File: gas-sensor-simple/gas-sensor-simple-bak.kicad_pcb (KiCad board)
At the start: 2 copper layers, 91.4 x 99.1 mm, 43 parts, among them J1 2x5 pin, J2 2x5 socket, J3 2x5 pin, J4 1x2, J5 1x2, J6 1x2, J7 1x2, U1 MQ-8, U10 RG LED, U12 LM393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

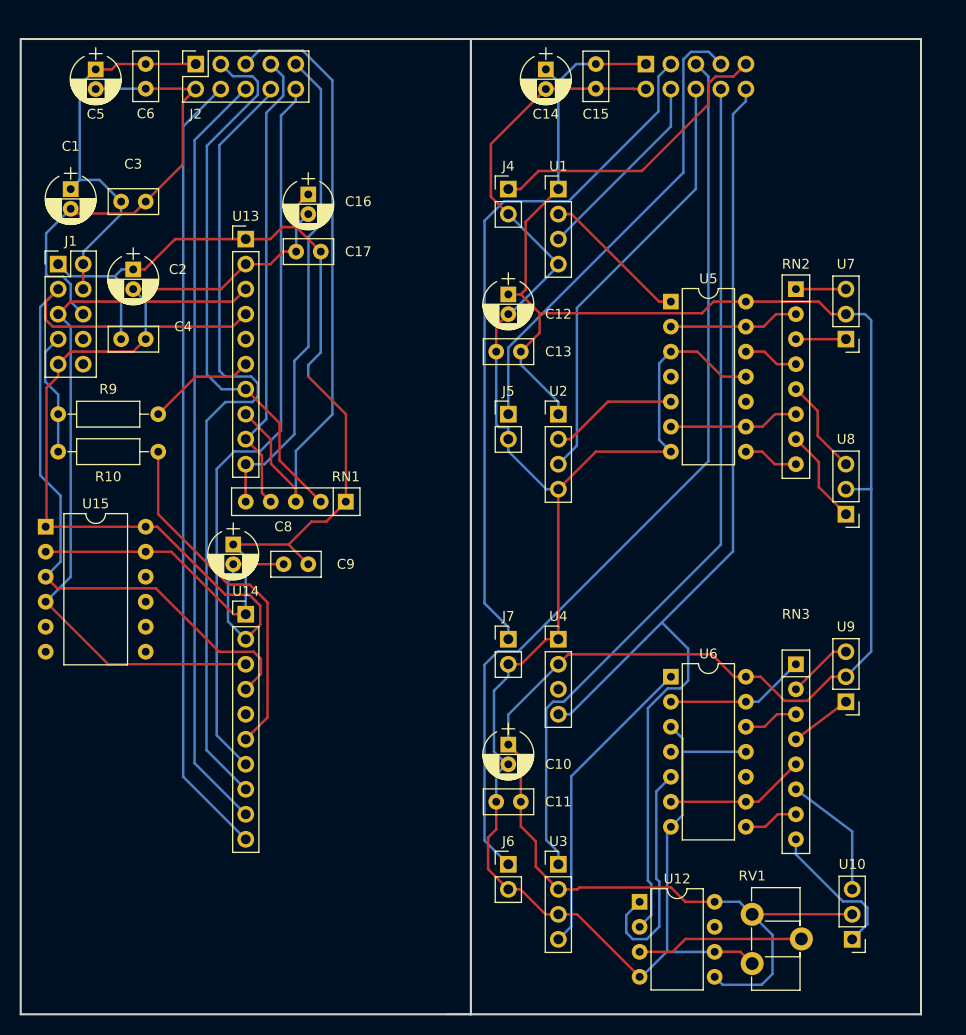
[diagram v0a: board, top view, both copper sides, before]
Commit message: Autorouted version 1 (gas-sensor-simple.kicad_pcb). Start work on version 2 layout (layout.kicad_pcb) moving RPi connector to top of digital board.
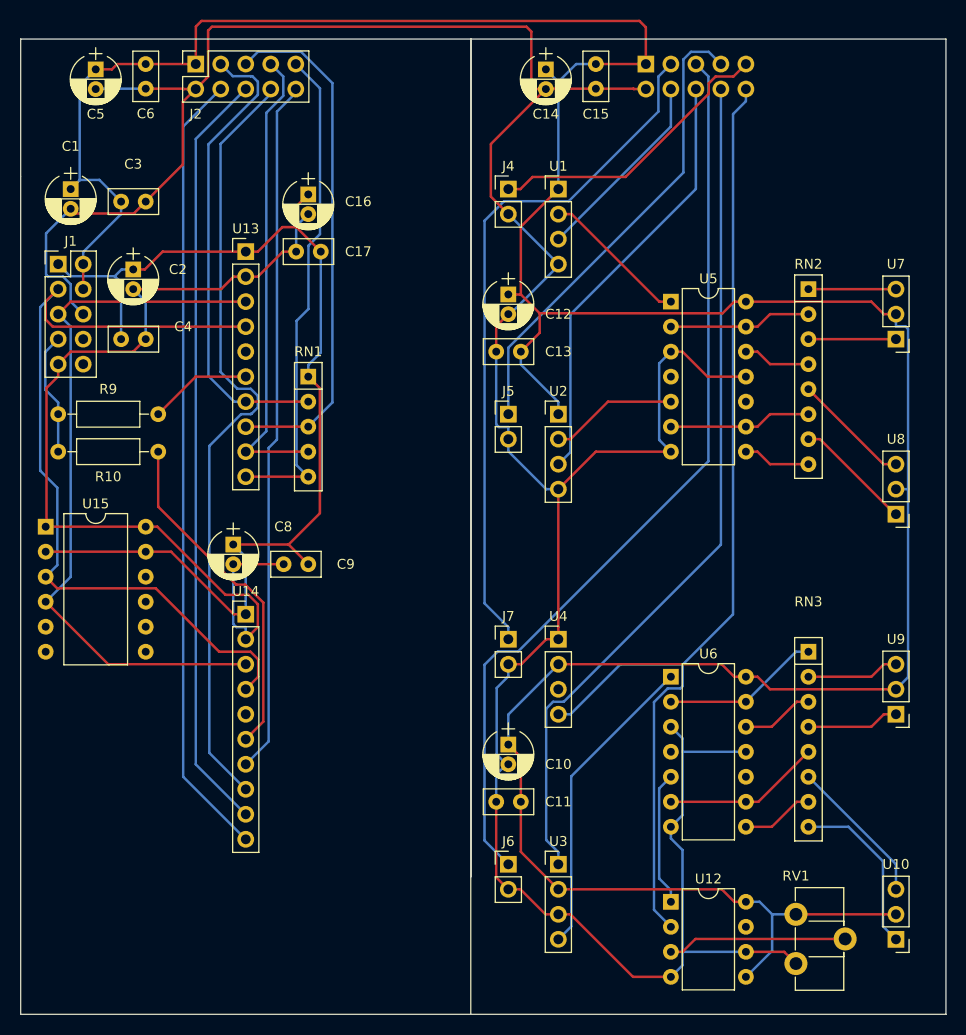
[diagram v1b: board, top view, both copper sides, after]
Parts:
- moved RN1 13.3 mm to (132.1, 85.1), turned to 270 degrees
- moved U9 5.24 mm to (191.8, 119.4)
- moved U7 5.08 mm to (191.8, 81.3)
- moved U8 5.08 mm to (191.8, 99.1)
- moved RV1 4.45 mm to (181.6, 139.7)
- moved U10 4.45 mm to (191.8, 142.2)
- moved U12 3.17 mm to (168.9, 138.4)
- moved RN3 1.80 mm to (182.9, 113.0)
- moved U13 1.27 mm to (125.7, 72.4)
- moved RN2 1.27 mm to (182.9, 76.2)
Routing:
- net VCC: track 269.4 -> 327.5 mm
- net GND: track 251.4 -> 300.7 mm
- net Net-(J2-Pad5): track 65.9 -> 52.9 mm
- net Net-(U12-Pad1): track 23.8 -> 13.7 mm
- net Net-(J2-Pad3): track 55.5 -> 47.7 mm
- net Net-(J2-Pad10): track 74.6 -> 70.7 mm
- net Net-(RN2-Pad3): track 5.08 -> 8.89 mm
- net Net-(RN2-Pad1): track 5.08 -> 8.89 mm
- net +3V3: track 114.9 -> 111.9 mm
- net Net-(RN3-Pad4): track 6.35 -> 9.42 mm
- net Net-(RN3-Pad2): track 6.66 -> 9.42 mm
- net Net-(RN3-Pad8): track 14.9 -> 17.5 mm
- net Net-(RN2-Pad7): track 9.73 -> 12.0 mm
- net Net-(RN2-Pad5): track 9.73 -> 12.0 mm
- net Net-(RN3-Pad6): track 13.0 -> 15.1 mm
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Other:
- board size 91.4 x 99.1 mm -> 94 x 99.1 mm
- net class Default: trace_width 0.254 -> 0.381
- board text removed: "1.0"
- board text removed: "2017-11-14"
- board text removed: "Analog gas sensor and digital interface"
- board text removed: "Gas Sensor v1"
